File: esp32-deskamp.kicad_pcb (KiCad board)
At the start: 2 copper layers, 140.2 x 66.5 mm, 33 parts, among them J1 INPUT 00, J10 ADDITIONAL GPIO, J2 INPUT 01, J3 MUTE, J4 SLEEP, J5 PRE OUT, J6 LFE OUT, J7 INPUT SELECT, J8 MOTOR, J9 12V IN, K1 INPUT 00, K2 INPUT 01, K3 AMP MUTE, K4 AMP SLEEP, U1 ESP32 D1 MINI, U2 TSR 1-2433, U3 L9110, U4 ULN2003A

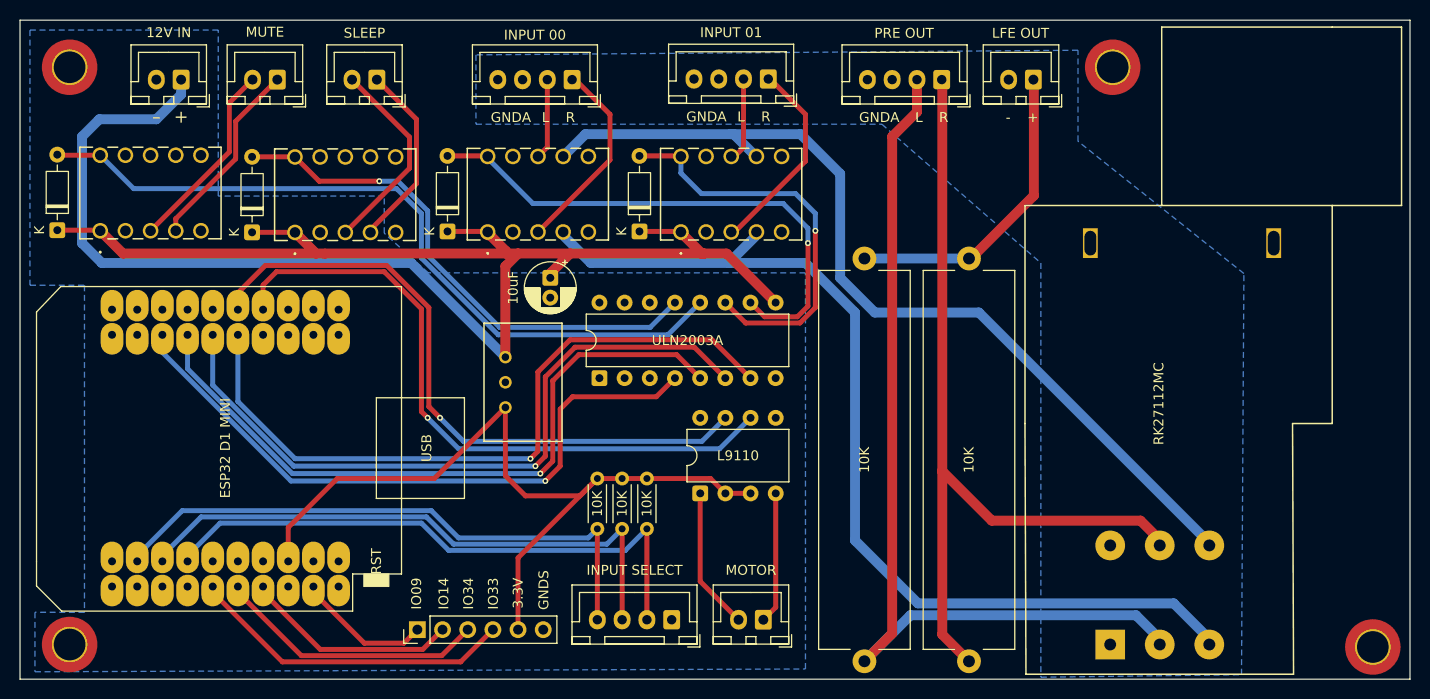
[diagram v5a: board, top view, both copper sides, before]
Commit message: Fix edge cuts
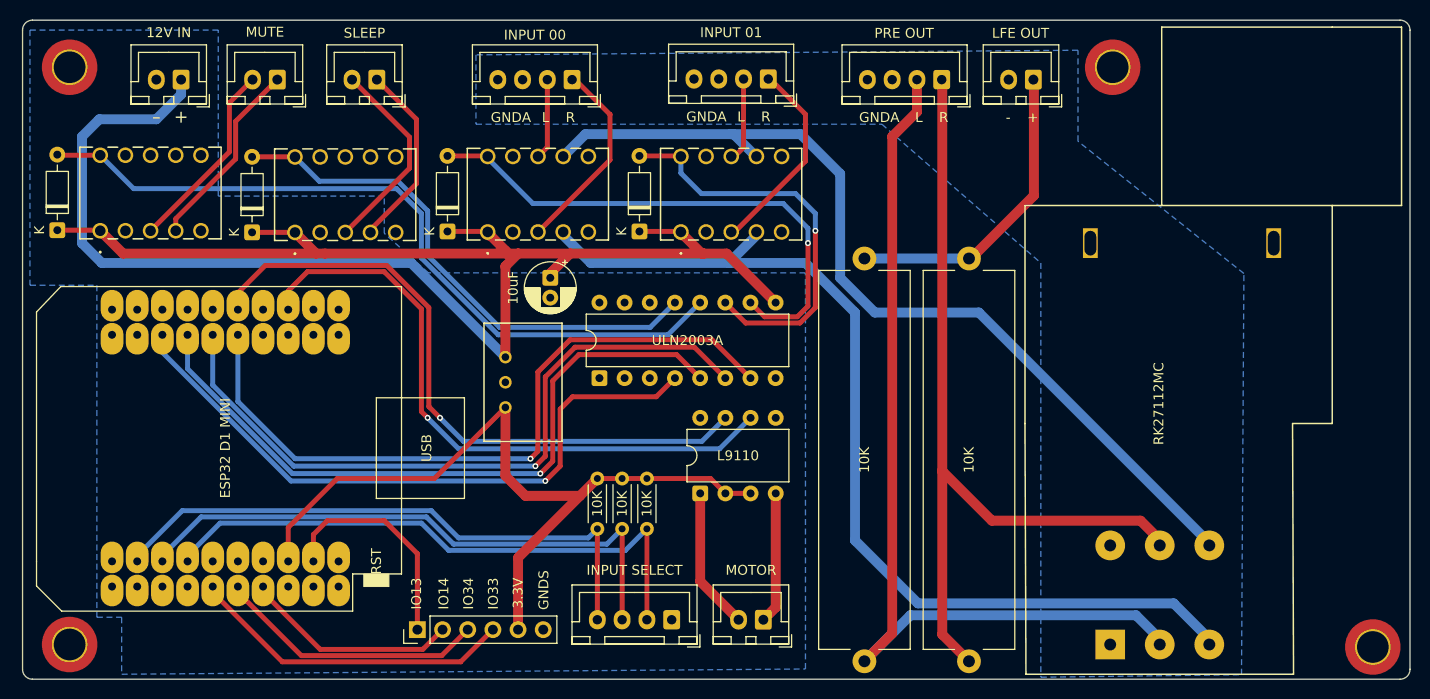
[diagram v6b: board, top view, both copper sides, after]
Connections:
- U1 pad 17: IO1 -> unconnected-(U1-IO_09/SD2-Pad17)
- U1 pad 18: unconnected-(U1-IO_13/TCK-Pad18) -> IO1
- U1 pad 34: PWM0 -> unconnected-(U1-IO_00-Pad34)
- U1 pad 36: unconnected-(U1-IO_02-Pad36) -> PWM0
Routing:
- net IO1: track 13.2 -> 22.8 mm
- net PWM0: track 67.0 -> 64.1 mm
- net Relay3: vias 1 -> 0
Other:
- board size 140.2 x 66.5 mm -> 140 x 66.5 mm
- board text added: "IO13"
- board text removed: "IO09"

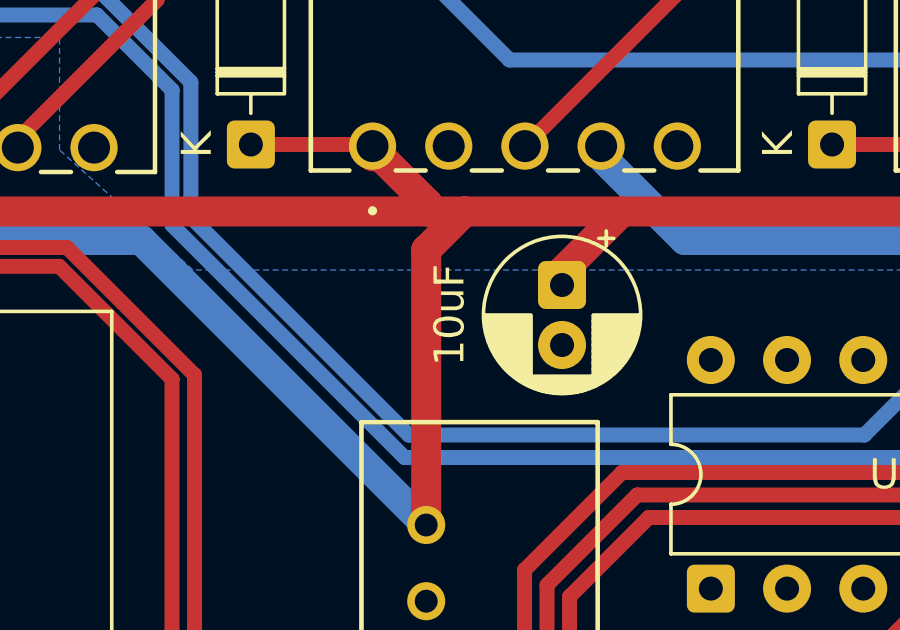
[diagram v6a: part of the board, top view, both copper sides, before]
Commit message: Change to proper µ symbol
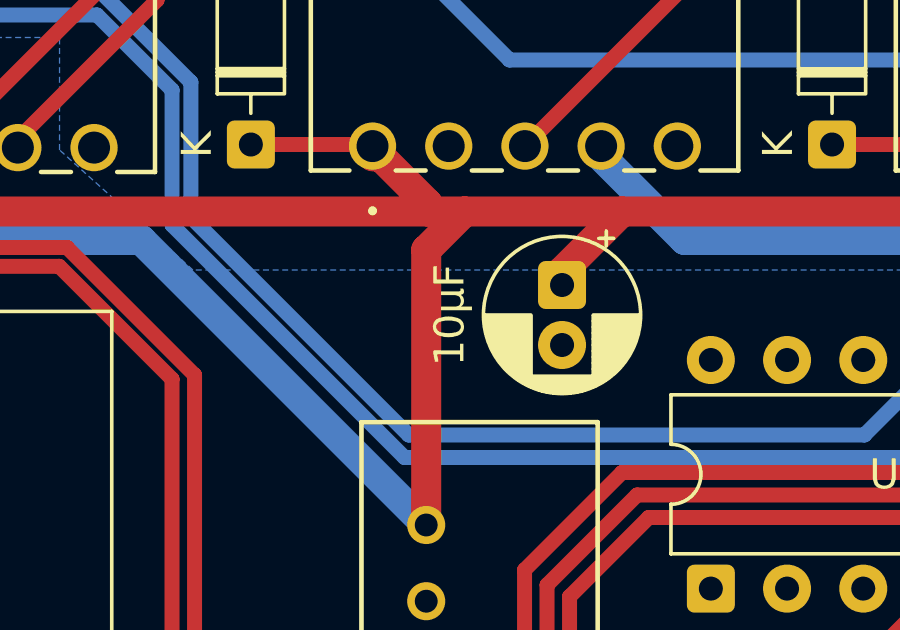
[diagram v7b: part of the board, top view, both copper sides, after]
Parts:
- C1: value 10uF -> 10µF
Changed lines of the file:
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@@
 			)
 		)
-		(property "Value" "10uF"
+		(property "Value" "10µF"
 			(at 1 3.75 90)
 			(layer "F.SilkS")
